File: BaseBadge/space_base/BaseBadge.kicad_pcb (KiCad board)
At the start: 2 copper layers, 116.7 x 74.5 mm, 8 parts, among them J1 Conn_02x03_Counter_Clockwise, J2 Conn_02x03_Counter_Clockwise, J3 Conn_02x03_Counter_Clockwise, J4 Conn_02x03_Counter_Clockwise, J5 Conn_02x03_Counter_Clockwise, SW1 SW_SPDT

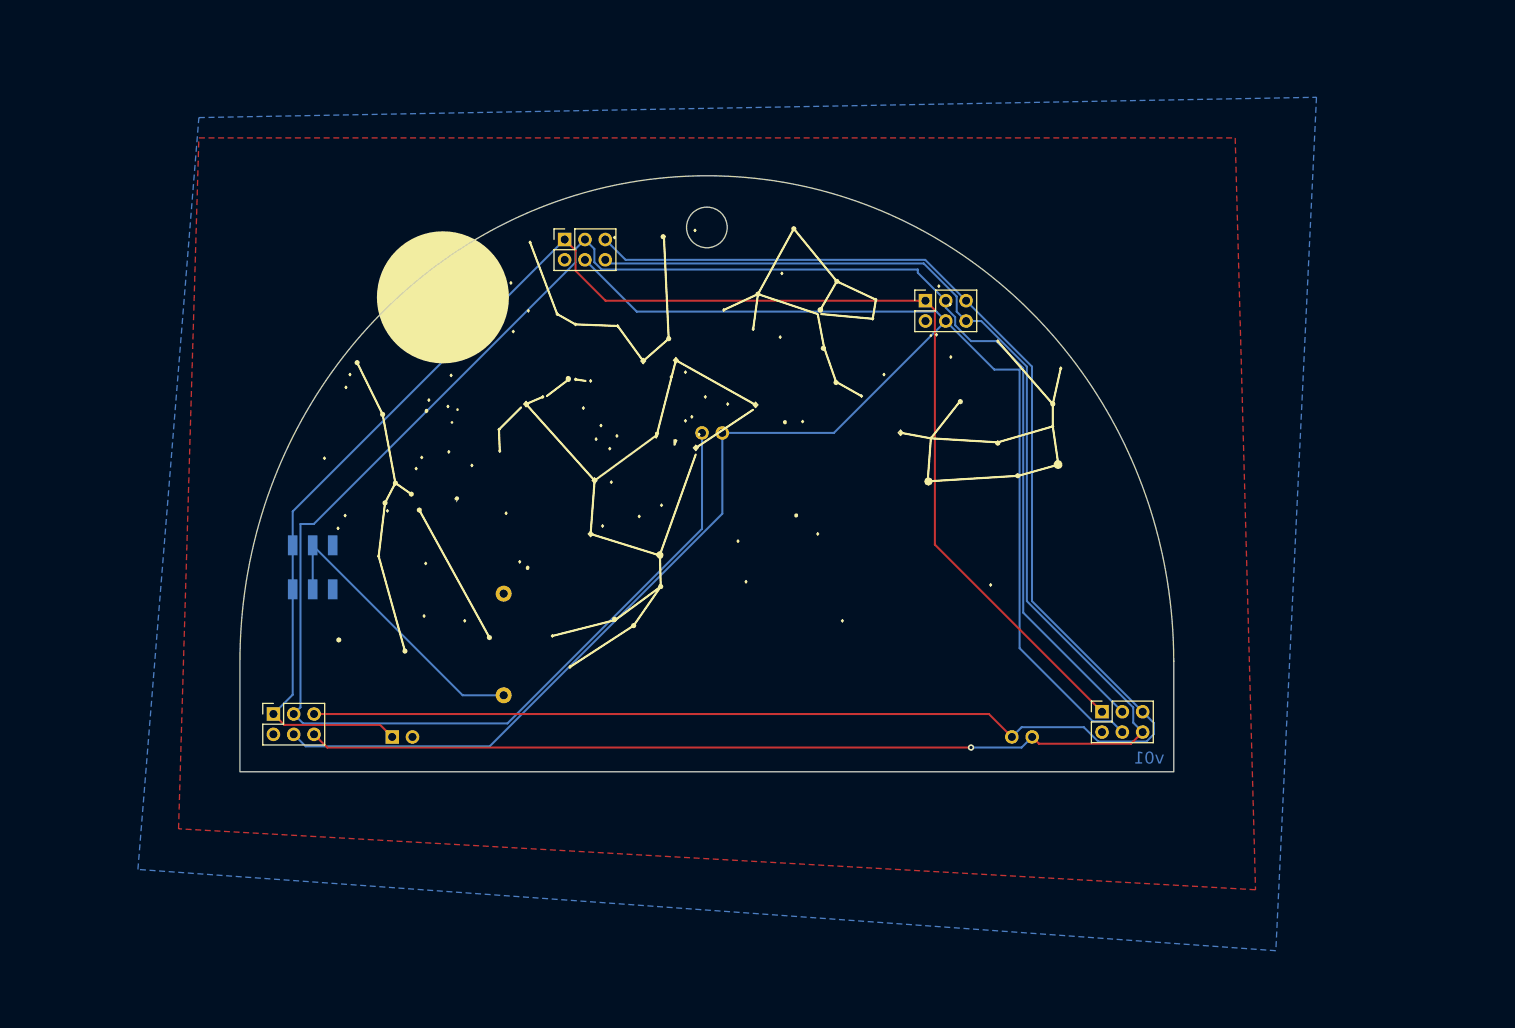
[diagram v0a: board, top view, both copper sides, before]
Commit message: overhauls across boards to v02
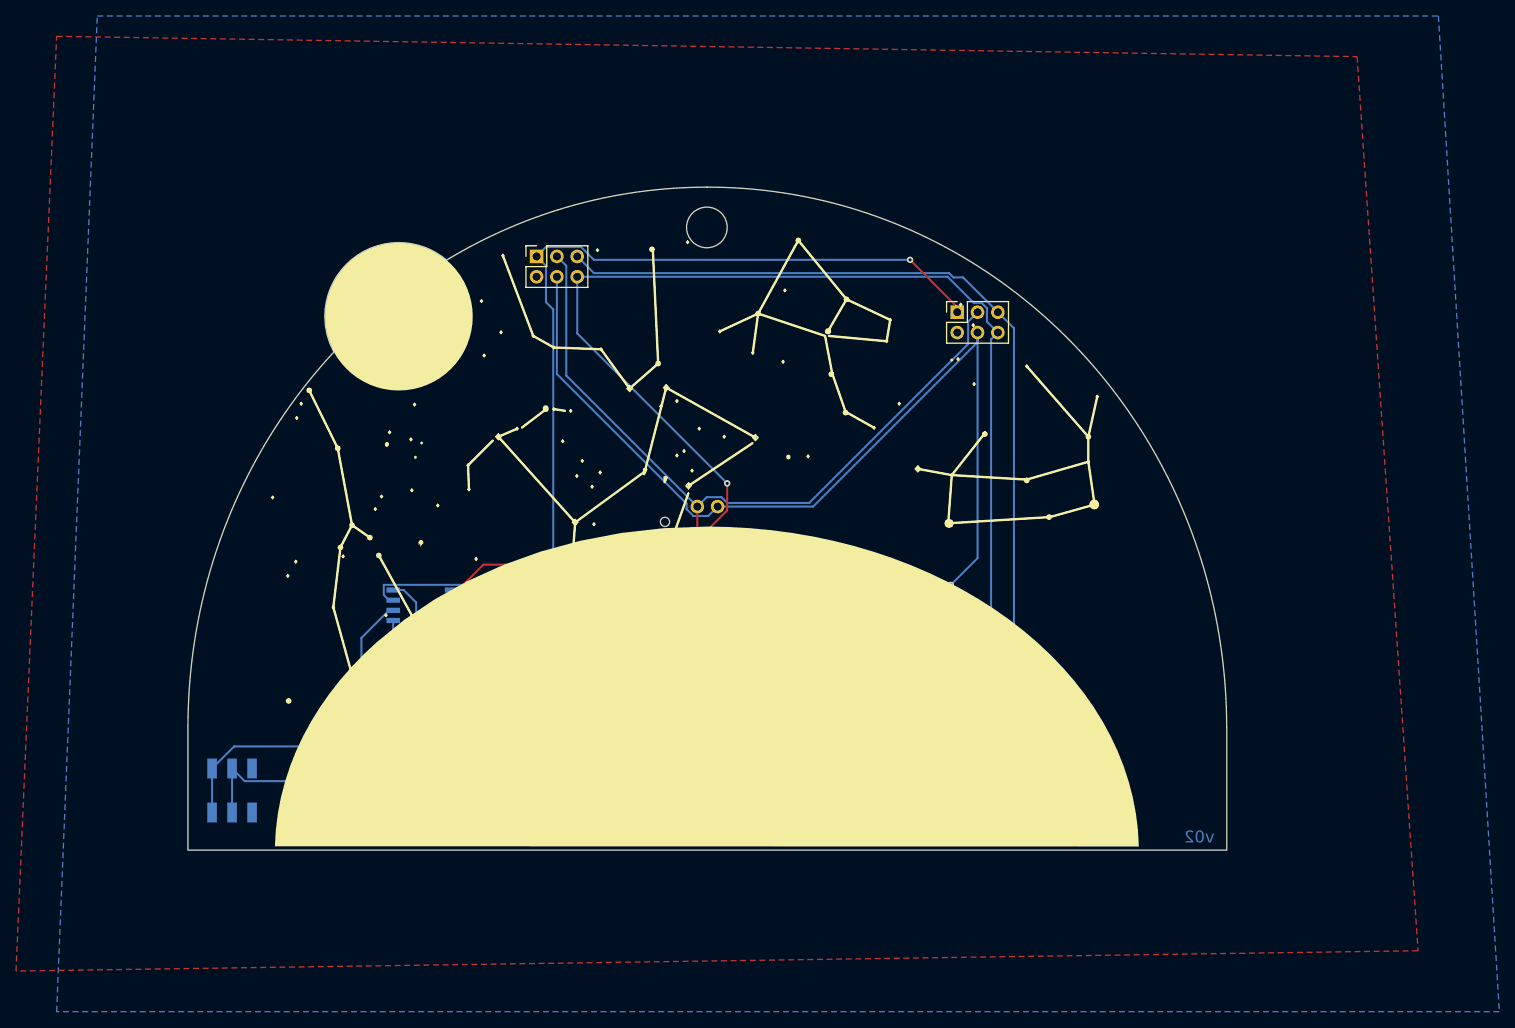
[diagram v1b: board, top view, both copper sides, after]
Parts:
- removed J4, J5: Conn_02x03_Counter_Clockwise, Connector_PinSocket_2.54mm:PinSocket_2x03_P2.54mm_Vertical
- removed the svg2mod at (144.5, 88.9)
- added ?: , , F.Cu at (179.7, 126.1)
- added ?: , , F.Cu at (142.1, 88.6)
- added C1: 10uf, Capacitor_SMD:C_0805_2012Metric, B.Cu at (109.9, 112.9)
- added C2: 10uf, Capacitor_SMD:C_0805_2012Metric, B.Cu at (109.9, 117.3)
- added REF**: SMT_Tooling_hole, aerospace_badge:SMT_Tooling_hole, F.Cu at (115.9, 124.9)
- added U1: ATtiny85-20S, Package_SO:SOIC-8W_5.3x5.3mm_P1.27mm, B.Cu at (111.8, 99.1)
- added VR1: HT7533-1, Package_TO_SOT_SMD:SOT-89-3, B.Cu at (104.6, 116.7)
- added svg2mod: G***, aerospace_badge:space_base, F.Cu at (149.6, 97.3)
- added svg2mod: G***, aerospace_badge:aerospace_logo_new, B.Cu at (109.3, 61.1)
- moved J2 66.0 mm to (126.0, 55.5)
- moved SW1 29.7 mm to (88.0, 122.2)
- moved BT1 9.97 mm to (123.8, 112.4)
- moved J1 9.23 mm to (147.4, 124.7)
- moved J3 4.23 mm to (178.6, 62.4)
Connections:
- SW1 pad 1: VCC -> Net-(C1-Pad1)
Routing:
- net Net-(J1-Pad3): track 260.8 -> 135.6 mm, vias 0 -> 1
- net Net-(C1-Pad1): track 0.00 -> 32.3 mm
- net Net-(J1-Pad4): track 222.1 -> 189.8 mm, vias 0 -> 2
- net VCC: track 200.7 -> 179.6 mm, vias 0 -> 3
- net Net-(J1-Pad6): track 216.8 -> 200.4 mm, vias 1 -> 2
- net Net-(BT1-Pad1): track 37.1 -> 42.4 mm
- net Net-(J1-Pad5): track 220.0 -> 216.1 mm, vias 0 -> 1
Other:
- board size 116.7 x 74.5 mm -> 129.9 x 82.9 mm
- board text added: "Aerospace Village"
- board text added: "Art flysurreal.com"
- board text added: "DEFCON 30"
- board text added: "Designed by: @cybertestpilot"
- board text added: "v02"
- board text removed: "v01"

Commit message: added artwork to back of base badge
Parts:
- added R1: 4.7K, Resistor_SMD:R_0805_2012Metric, B.Cu at (103.0, 97.2)
- added R2: 4.7K, Resistor_SMD:R_0805_2012Metric, B.Cu at (98.2, 97.2)
- added svg2mod: G***, aerospace_badge:defcon_30_logo, F.Cu at (188.0, 50.8)
- added svg2mod: G***, aerospace_badge:defcon_30_logo, F.Cu at (177.8, 43.2)
- added svg2mod: G***, aerospace_badge:defcon_30_logo, B.Cu at (104.8, 86.1)
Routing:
- net VCC: track 179.6 -> 206.5 mm
- net Net-(J1-Pad3): track 135.6 -> 154.8 mm
- net Net-(J1-Pad4): track 189.8 -> 194.6 mm
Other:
- board text added: "@SecureAerospace"
- board text added: "SAO Enhancements"
- board text added: "aerospacevillage.org"
- board text added: "v03"
- board text removed: "DEFCON 30"
- board text removed: "v02"

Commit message: updated base badge, shuttle, and warning
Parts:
- removed the svg2mod at (188.0, 50.8)
- removed the svg2mod at (177.8, 43.2)
- added J4: AVR-ISP-6, aerospace_badge:AVR-ISP-6, B.Cu at (118.0, 105.3)
- moved svg2mod 5.67 mm to (108.3, 81.7)
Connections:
- U1 pad 1: unconnected-(U1-Pad1) -> Net-(U1-Pad1)
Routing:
- net Net-(J1-Pad4): track 194.6 -> 212.9 mm
- net Net-(U1-Pad1): track 0.00 -> 17.4 mm, vias 0 -> 1
- net Net-(J1-Pad5): track 216.1 -> 227.4 mm
- net Net-(J1-Pad3): track 154.8 -> 162.6 mm
- net VCC: track 206.5 -> 211.0 mm
- net GND: vias 0 -> 1
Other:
- board text added: "BUILD INSPIRE PROMOTE"
- board text added: "ISP"

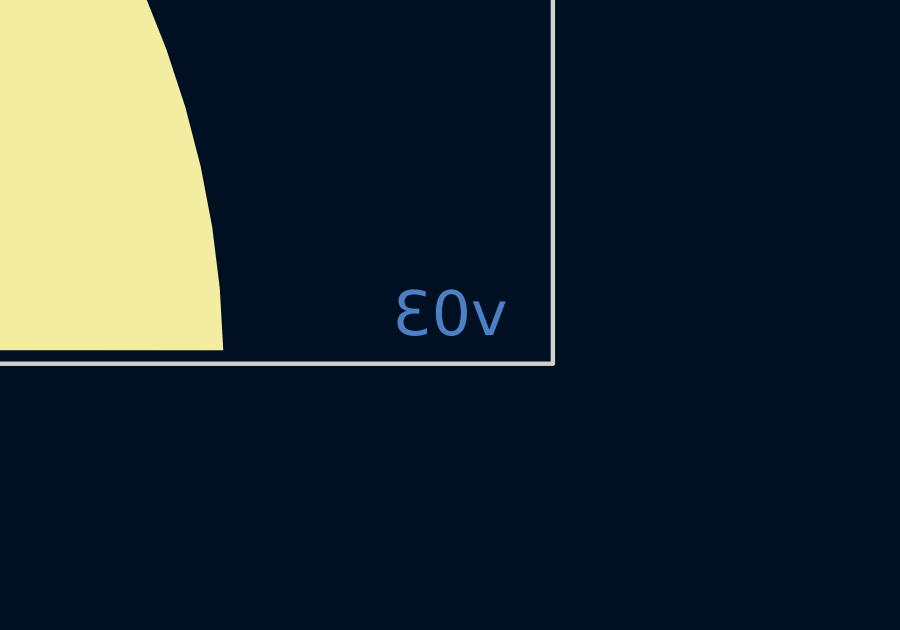
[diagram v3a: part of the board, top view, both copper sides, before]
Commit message: added Registered trademark thing
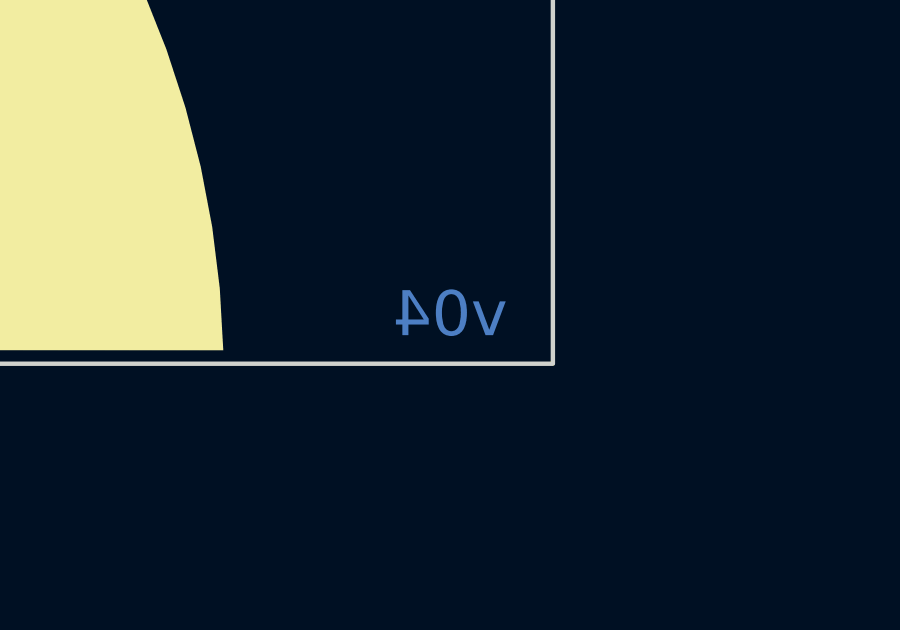
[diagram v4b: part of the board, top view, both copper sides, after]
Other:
- board text added: "v04"
- board text added: "®"
- board text removed: "v03"
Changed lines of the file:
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@@
   (title_block
     (title "Aerospace Village Base Badge 2022")
-    (date "2022-05-26")
-    (rev "v03")
+    (date "2022-06-01")
+    (rev "v04")
     (company "Author: Dan Allen")
   )
@@
   (gr_poly
     (pts
-      (xy 157.790069 66.822655)
-      (xy 157.616691 67.007824)
-      (xy 157.443321 67.192993)
-      (xy 157.385528 67.197693)
-      (xy 157.385452 67.197708)
-      (xy 157.327659 67.202408)
-      (xy 157.331962 67.144619)
-      (xy 157.336265 67.08683)
-      (xy 157.563171 66.907601)
-      (xy 157.790069 66.728367)
-    ) (layer "B.SilkS") (width 0) (fill solid))
-  (gr_poly
-    (pts
       (xy 130.872375 78.169373)
       (xy 130.923744 78.220742)
@@
   (gr_poly
     (pts
+      (xy 158.098289 67.279454)
+      (xy 158.064308 67.279454)
+      (xy 158.030342 67.279343)
+      (xy 157.982719 67.202294)
+      (xy 157.935096 67.125233)
+      (xy 158.098289 67.125233)
+    ) (layer "B.SilkS") (width 0) (fill solid))
+  (gr_poly
+    (pts
       (xy 157.63594 55.336659)
       (xy 157.558883 55.336659)
@@
   (gr_poly
     (pts
-      (xy 155.94075 67.202412)
-      (xy 155.863693 67.202412)
-      (xy 155.863693 67.125355)
-      (xy 155.94075 67.125355)
-    ) (layer "B.SilkS") (width 0) (fill solid))
-  (gr_poly
-    (pts
       (xy 150.803875 76.294037)
       (xy 150.5984 76.294037)
@@
   (gr_poly
     (pts
+      (xy 157.790069 66.822655)
+      (xy 157.616691 67.007824)
+      (xy 157.443321 67.192993)
+      (xy 157.385528 67.197693)
+      (xy 157.385452 67.197708)
+      (xy 157.327659 67.202408)
+      (xy 157.331962 67.144619)
+      (xy 157.336265 67.08683)
+      (xy 157.563171 66.907601)
+      (xy 157.790069 66.728367)
+    ) (layer "B.SilkS") (width 0) (fill solid))
+  (gr_poly
+    (pts
       (xy 139.68227 71.773735)
       (xy 139.630901 71.722367)
@@
   (gr_poly
     (pts
-      (xy 158.098289 67.279454)
-      (xy 158.064308 67.279454)
-      (xy 158.030342 67.279343)
-      (xy 157.982719 67.202294)
-      (xy 157.935096 67.125233)
-      (xy 158.098289 67.125233)
-    ) (layer "B.SilkS") (width 0) (fill solid))
-  (gr_poly
-    (pts
       (xy 133.363815 77.989884)
       (xy 133.286758 77.989884)
@@
   (gr_poly
     (pts
+      (xy 155.94075 67.202412)
+      (xy 155.863693 67.202412)
+      (xy 155.863693 67.125355)
+      (xy 155.94075 67.125355)
+    ) (layer "B.SilkS") (width 0) (fill solid))
+  (gr_poly
+    (pts
       (xy 145.178882 74.753159)
       (xy 144.973407 74.753159)
@@
     ) (layer "B.Mask") (width 0) (fill solid))
   (gr_circle (center 147.319999 51.828999) (end 149.859999 51.828999) (layer "Edge.Cuts") (width 0.1) (fill none))
-  (gr_text "v03" (at 208.877118 128.021104) (layer "B.Cu")
+  (gr_text "v04" (at 208.877118 128.021104) (layer "B.Cu")
     (effects (font (size 1.5 1.5) (thickness 0.3)) (justify mirror))
   )
@@
     (effects (font (size 1 1) (thickness 0.15)) (justify mirror))
   )
+  (gr_text "®" (at 100.211407 85.138733) (layer "B.Mask")
+    (effects (font (size 1 1) (thickness 0.25)) (justify mirror))
+  )
   (segment (start 87.97052 124.963928) (end 87.97052 119.463928) (width 0.254) (layer "B.Cu") (net 1))
